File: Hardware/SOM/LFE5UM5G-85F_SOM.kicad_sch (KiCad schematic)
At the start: 0 parts

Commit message: SOM: layout update
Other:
- sheet QSPI renamed QSPI (page 5)
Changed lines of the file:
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@@
 			(color 0 0 0 0.0000)
 		)
-		(property "Sheetname" "QSPI"
+		(property "Sheetname" "QSPI (page 5)"
 			(at 90.424 104.648 0)
 			(effects

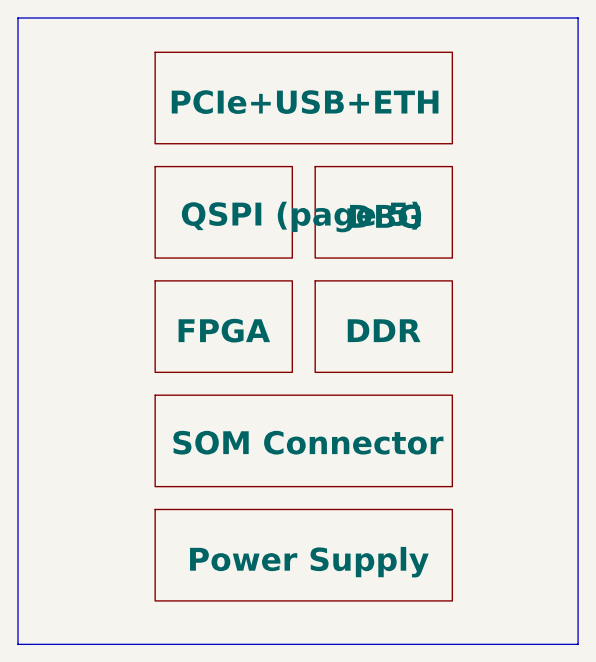
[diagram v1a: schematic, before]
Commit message: Switched to 8-layer stack-up JLC08161H-2116
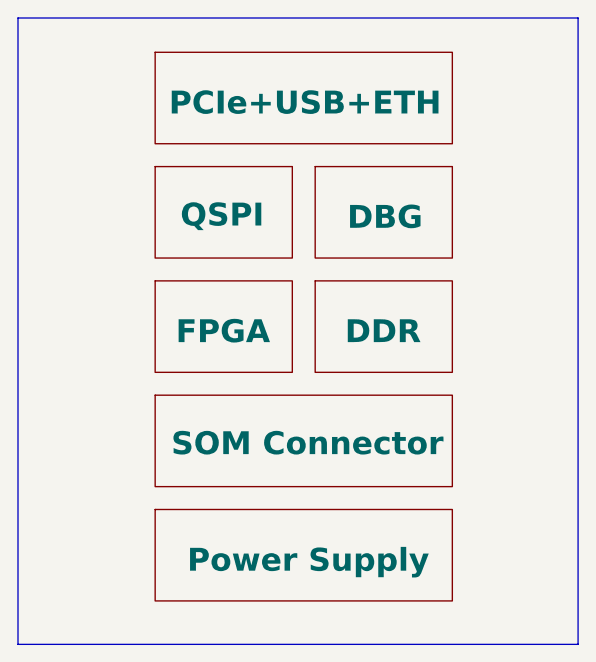
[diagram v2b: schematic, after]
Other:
- sheet QSPI (page 5) renamed QSPI
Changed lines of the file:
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@@
 			(color 0 0 0 0.0000)
 		)
-		(property "Sheetname" "QSPI (page 5)"
+		(property "Sheetname" "QSPI"
 			(at 90.424 104.648 0)
 			(effects
